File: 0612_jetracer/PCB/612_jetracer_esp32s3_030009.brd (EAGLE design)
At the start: 87.5 x 72 mm, 81 parts, among them Q3 MOSFET-N_FDN335N, Q4 MOSFET-N_FDN335N, Q5 MOSFET-N_FDN335N, T1 RN1401, T5 RN1401, U1 TLP291A

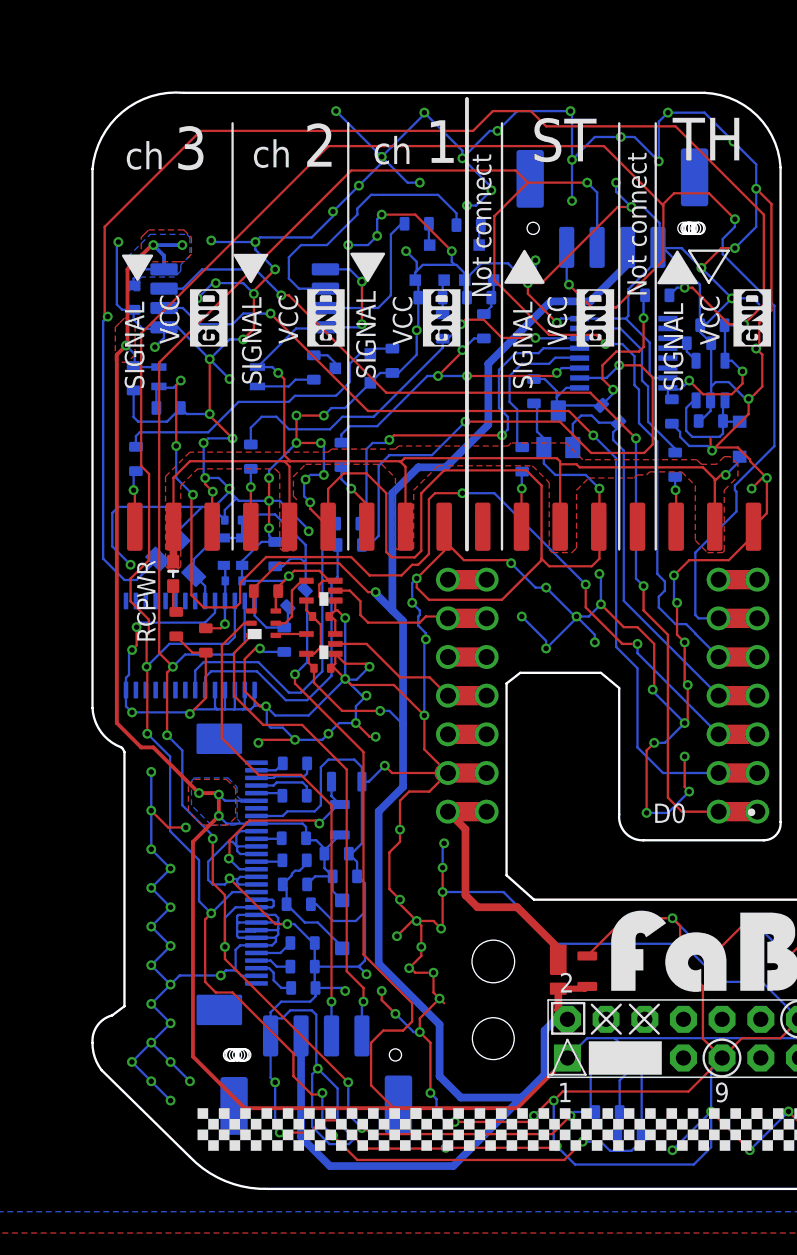
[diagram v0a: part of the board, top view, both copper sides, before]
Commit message: #612 JetRacer Rev3.0.9 製造時の不良を防止するためGND経路修正
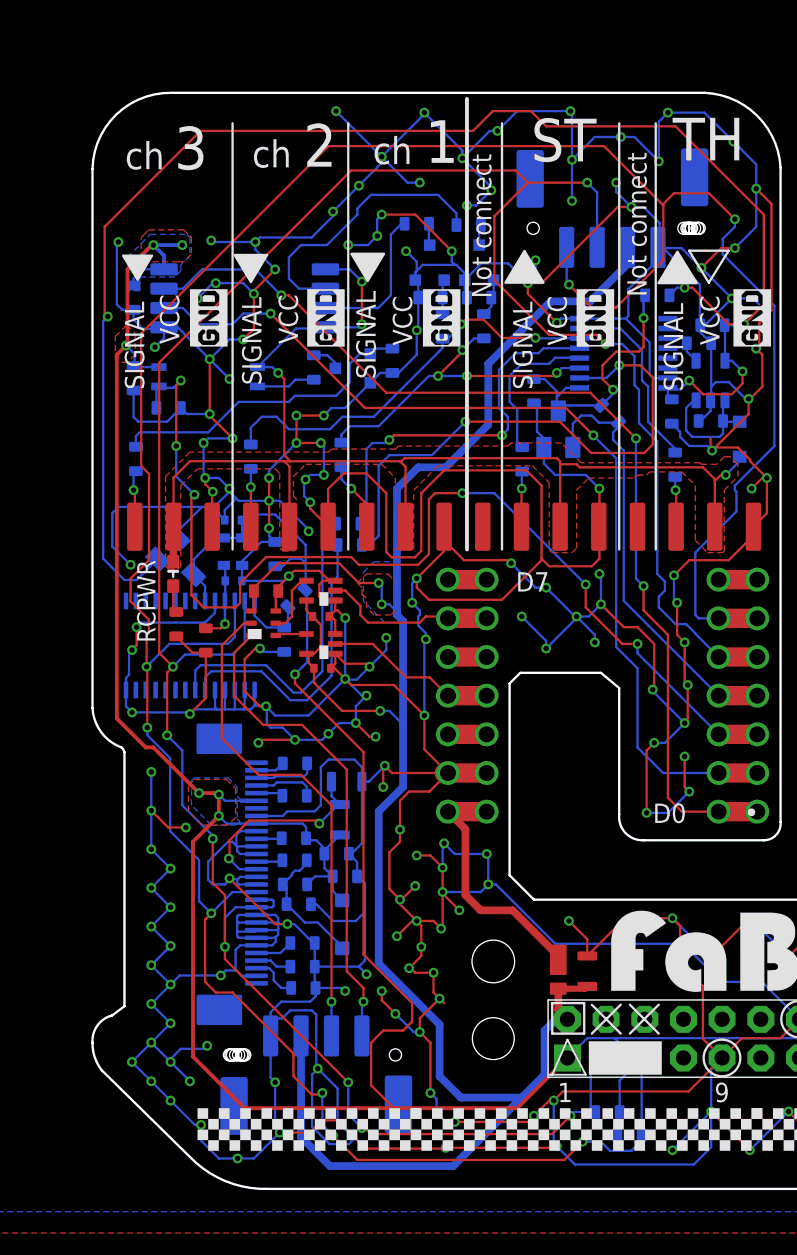
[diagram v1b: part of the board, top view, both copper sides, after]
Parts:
- added U$13: (no value), FaBo-Logo:LOGO_FABO_M_BOTTOM
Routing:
- net GND: track 1030.4 -> 1060.6 mm, vias 189 -> 200
- net 5V_JETSON: track 133.6 -> 134.3 mm, vias 2 -> 3
- added copper zone on layer 1, net 5V_JETSON
- added copper zone on layer 16, net 5V_JETSON
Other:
- outline, holes or cut-outs redrawn
- board text added: "D10"
- board text added: "D7"
- board text added: "ESC"
- board text added: "Receiver"
- board text added: "Servo"
- board text added: "VUSB"

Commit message: #612 JetRacer コントロール基板　Rev3.0.8,Rev3.0.9 追加修正箇所注釈追加。
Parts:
- R14: value 1K -> 4.７K
- R5: value 1K -> 4.7K
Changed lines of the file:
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@@
 <drawing>
 <settings>
-<setting alwaysvectorfont="no"/>
+<setting alwaysvectorfont="yes"/>
 <setting keepoldvectorfont="yes"/>
 <setting verticaltext="up"/>
@@
 <grid distance="0.1" unitdist="mm" unit="mm" style="lines" multiple="1" display="yes" altdistance="0.1" altunitdist="mm" altunit="mm"/>
 <layers>
-<layer number="1" name="Top" color="4" fill="1" visible="yes" active="yes"/>
+<layer number="1" name="Top" color="4" fill="1" visible="no" active="yes"/>
 <layer number="16" name="Bottom" color="1" fill="1" visible="yes" active="yes"/>
 <layer number="17" name="Pads" color="2" fill="1" visible="yes" active="yes"/>
@@
 <attribute name="VALUE" x="32.505" y="46.725" size="1.27" layer="28" rot="MR0"/>
 </element>
-<element name="R5" library="FaBo-Resistors" package="0603" value="1K" x="37.1" y="58.7" smashed="yes" rot="MR180">
+<element name="R5" library="FaBo-Resistors" package="0603" value="4.7K" x="37.1" y="58.7" smashed="yes" rot="MR180">
 <attribute name="NAME" x="37.1" y="57.95" size="0.8128" layer="126" font="vector" ratio="15" rot="MR180" align="bottom-center"/>
+<attribute name="SPICEPREFIX" value="R" x="37.1" y="58.7" size="1.778" layer="28" rot="MR180" display="off"/>
 <attribute name="VALUE" x="37" y="59.6" size="0.8128" layer="28" font="vector" ratio="15" rot="MR180" align="center"/>
 </element>
@@
 <attribute name="VALUE" x="2.207896875" y="42.098028125" size="1.27" layer="28" rot="MR135"/>
 </element>
-<element name="R14" library="FaBo-Resistors" package="0603" value="1K" x="13.4" y="38.8" smashed="yes" rot="MR315">
+<element name="R14" library="FaBo-Resistors" package="0603" value="4.７K" x="13.4" y="38.8" smashed="yes" rot="MR315">
 <attribute name="NAME" x="12.869671875" y="39.330328125" size="0.8128" layer="126" font="vector" ratio="15" rot="MR315" align="bottom-center"/>
 <attribute name="VALUE" x="13.9656875" y="38.092890625" size="0.8128" layer="28" font="vector" ratio="15" rot="MR315" align="center"/>

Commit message: #612 JetRacer Rev3.0.8B,Rev3.0.9 リリース
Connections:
- removed net 3V3: C2.2, IC2.28, R14.2
- net 3V3_JETSON: now also C2.2, IC2.28, R14.2
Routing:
- net 3V3_JETSON: track 201.9 -> 208.3 mm
- net 3V3: track 4.70 -> 0.00 mm
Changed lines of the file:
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@@
 <drawing>
 <settings>
-<setting alwaysvectorfont="yes"/>
+<setting alwaysvectorfont="no"/>
 <setting keepoldvectorfont="yes"/>
 <setting verticaltext="up"/>
@@
 <grid distance="0.1" unitdist="mm" unit="mm" style="lines" multiple="1" display="yes" altdistance="0.1" altunitdist="mm" altunit="mm"/>
 <layers>
-<layer number="1" name="Top" color="4" fill="1" visible="no" active="yes"/>
+<layer number="1" name="Top" color="4" fill="1" visible="yes" active="yes"/>
 <layer number="16" name="Bottom" color="1" fill="1" visible="yes" active="yes"/>
 <layer number="17" name="Pads" color="2" fill="1" visible="yes" active="yes"/>
@@
 <wire x1="14" y1="39.399996875" x2="13.9656875" y2="39.365684375" width="0.1524" layer="16"/>
 <wire x1="13.9656875" y1="39.365684375" x2="14.1" y2="39.231371875" width="0.1524" layer="16"/>
-<wire x1="14.1" y1="39.231371875" x2="14.1" y2="34.6" width="0.1524" layer="16"/>
+<wire x1="14.1" y1="39.231371875" x2="14.1" y2="37.3" width="0.1524" layer="16"/>
+<wire x1="14.1" y1="37.3" x2="14.1" y2="34.6" width="0.1524" layer="16"/>
 <wire x1="34.3" y1="9.9" x2="50.22" y2="9.9" width="0.1524" layer="16"/>
 <wire x1="50.22" y1="9.9" x2="51.52" y2="8.6" width="0.1524" layer="16"/>
@@
 <wire x1="13" y1="41.4" x2="13.7" y2="41.4" width="0.1524" layer="16"/>
 <wire x1="13.7" y1="41.4" x2="14" y2="41.1" width="0.1524" layer="16"/>
+<contactref element="C2" pad="2"/>
+<contactref element="IC2" pad="28"/>
+<contactref element="R14" pad="2"/>
+<wire x1="12.834315625" y1="38.2343125" x2="12.834315625" y2="37.112715625" width="0.1524" layer="16"/>
+<wire x1="12.834315625" y1="37.112715625" x2="12.6608" y2="36.9392" width="0.1524" layer="16"/>
+<wire x1="12.6608" y1="36.9392" x2="12.596" y2="36.8744" width="0.1524" layer="16"/>
+<wire x1="12.834315625" y1="38.2343125" x2="13.168628125" y2="37.9" width="0.1524" layer="16"/>
+<wire x1="13.168628125" y1="37.9" x2="13.5" y2="37.9" width="0.1524" layer="16"/>
+<wire x1="13.5" y1="37.9" x2="14.1" y2="37.3" width="0.1524" layer="16"/>
+<wire x1="10.65" y1="38.62" x2="10.65" y2="37.65" width="0.1524" layer="16"/>
+<wire x1="11.3608" y1="36.9392" x2="12.6608" y2="36.9392" width="0.1524" layer="16"/>
+<wire x1="10.65" y1="37.65" x2="11.3608" y2="36.9392" width="0.1524" layer="16"/>
 </signal>
 <signal name="RCH1">
@@
 <contactref element="LED1" pad="VCC"/>
 <contactref element="C1" pad="2"/>
-<wire x1="10.6" y1="39.27" x2="10.6" y2="38.12" width="0.1524" layer="1"/>
-<wire x1="10.6" y1="38.12" x2="10.44" y2="37.96" width="0.1524" layer="1"/>
 <contactref element="SPI-LED" pad="5V"/>
 <wire x1="14.45" y1="37.6" x2="14.05" y2="38" width="0.1524" layer="1"/>
@@
 <vertex x="17.8" y="39"/>
 </polygon>
+<wire x1="10.44" y1="37.96" x2="10.6" y2="38.12" width="0.1524" layer="1"/>
+<wire x1="10.6" y1="38.12" x2="10.6" y2="39.27" width="0.1524" layer="1"/>
 </signal>
 <signal name="XAIO_5V">
@@
 <wire x1="29.7" y1="53.2" x2="30.5" y2="52.4" width="0.1524" layer="16"/>
 </signal>
-<signal name="3V3">
-<contactref element="C2" pad="2"/>
-<contactref element="IC2" pad="28"/>
-<wire x1="12.596" y1="36.8744" x2="11.4256" y2="36.8744" width="0.1524" layer="16"/>
-<wire x1="10.65" y1="37.65" x2="10.65" y2="38.62" width="0.1524" layer="16"/>
-<wire x1="11.4256" y1="36.8744" x2="10.65" y2="37.65" width="0.1524" layer="16"/>
-<contactref element="R14" pad="2"/>
-<wire x1="12.596" y1="36.8744" x2="12.834315625" y2="37.112715625" width="0.1524" layer="16"/>
-<wire x1="12.834315625" y1="38.2343125" x2="12.834315625" y2="37.112715625" width="0.1524" layer="16"/>
-</signal>
 </signals>

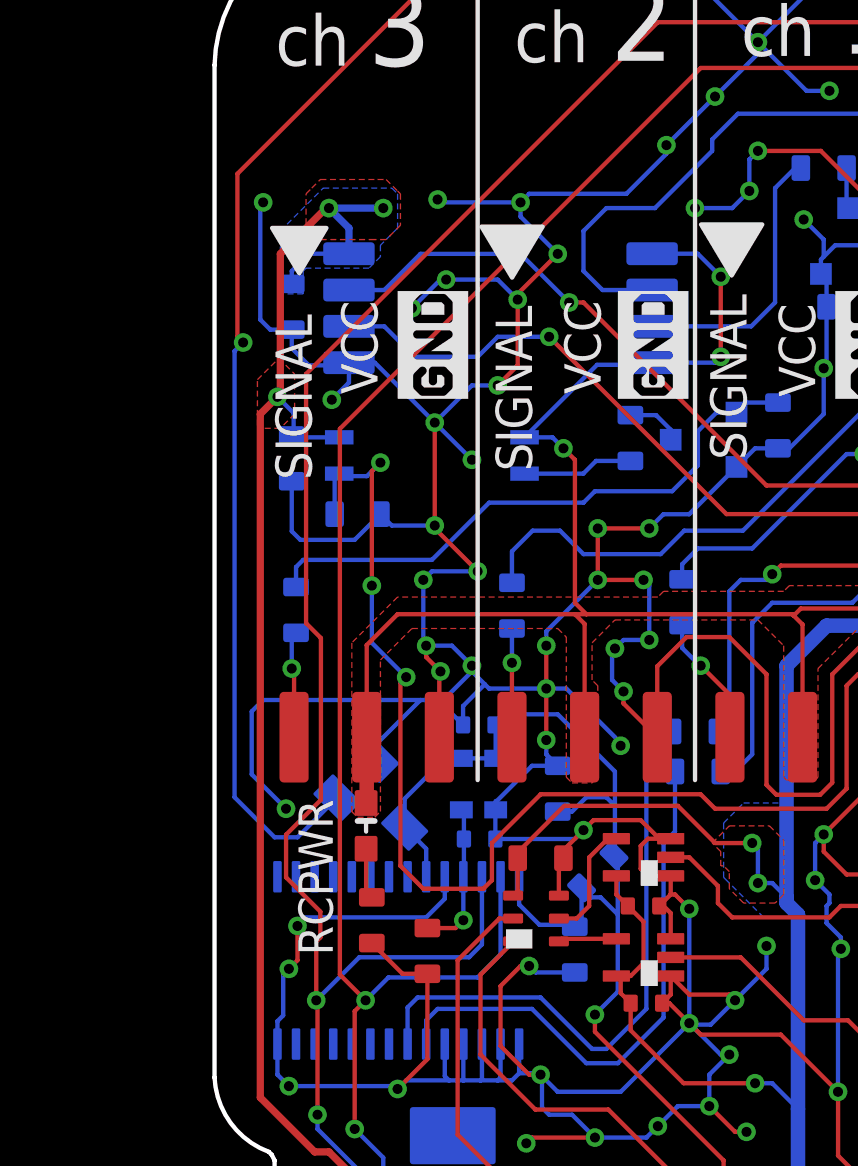
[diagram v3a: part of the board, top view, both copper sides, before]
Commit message: JetRacer Rev3.0.8　PCA9685 OEラインシンボル間違い修正しました。
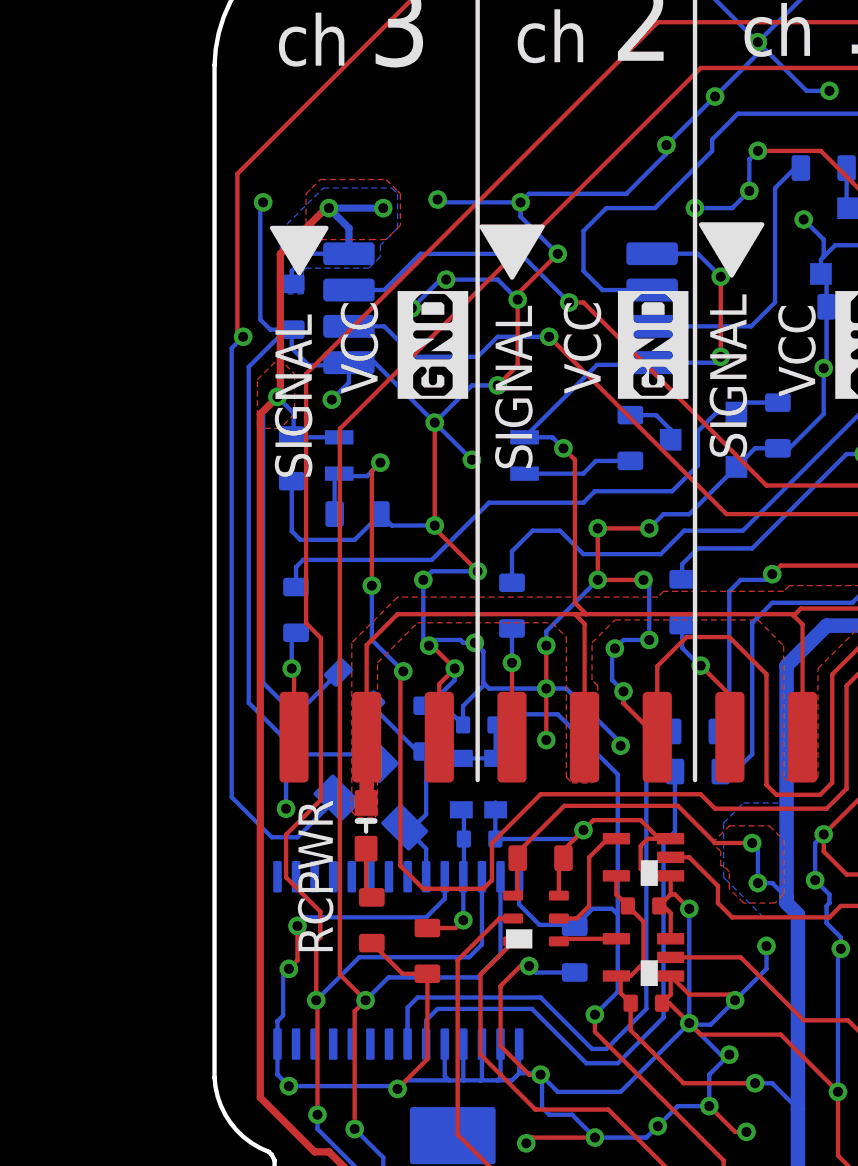
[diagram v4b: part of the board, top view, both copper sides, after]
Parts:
- moved R14 10.6 mm to (4.90, 45.2), turned to 45 degrees
- moved R3 5.06 mm to (7.40, 43.8)
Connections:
- new net OE: IC2.23, R14.1, R3.2, T1.C
- net 3V3_JETSON: no longer IC2.23, R14.1, R3.2, T1.C
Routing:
- net OE: track 0.00 -> 7.76 mm
- net 3V3_JETSON: track 208.3 -> 213.0 mm
- net GND: track 1060.6 -> 1064.4 mm
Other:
- board text added: "#612 JetRacer Rev 3.0.9 B 2024/11/29 Jetson Nano compatible"
- board text added: "CUHS20S30"
- board text added: "F-612-3-0-9-A-N-J-2-WAY"
- board text added: "Rev 3.0.9 B"
- board text removed: "#612 JetRacer Rev 3.0.9 2024/11/19 Jetson Nano compatible"
- board text removed: "F-612-3-0-9-A-N-J-1-WAY"
